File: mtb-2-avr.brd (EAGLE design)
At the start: 27 x 22 mm, 17 parts, among them IC1 MEGA8A-AU, Q1 14.745 MHz

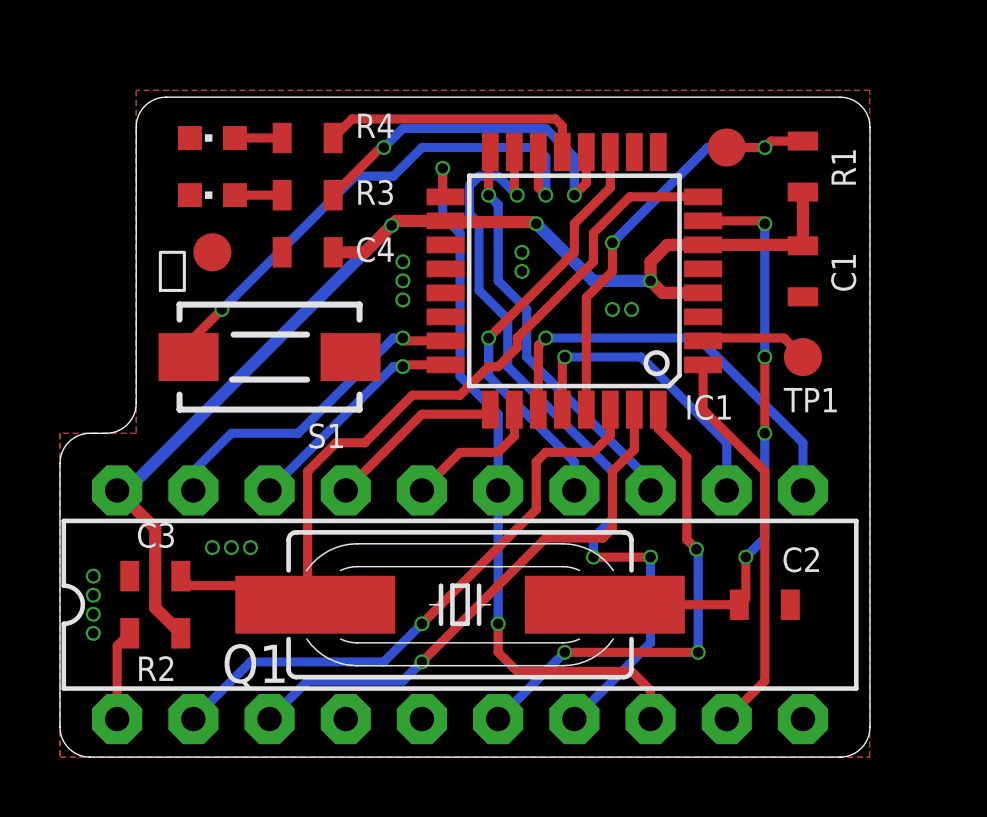
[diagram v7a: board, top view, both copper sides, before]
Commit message: Add possibility for THT crystal.
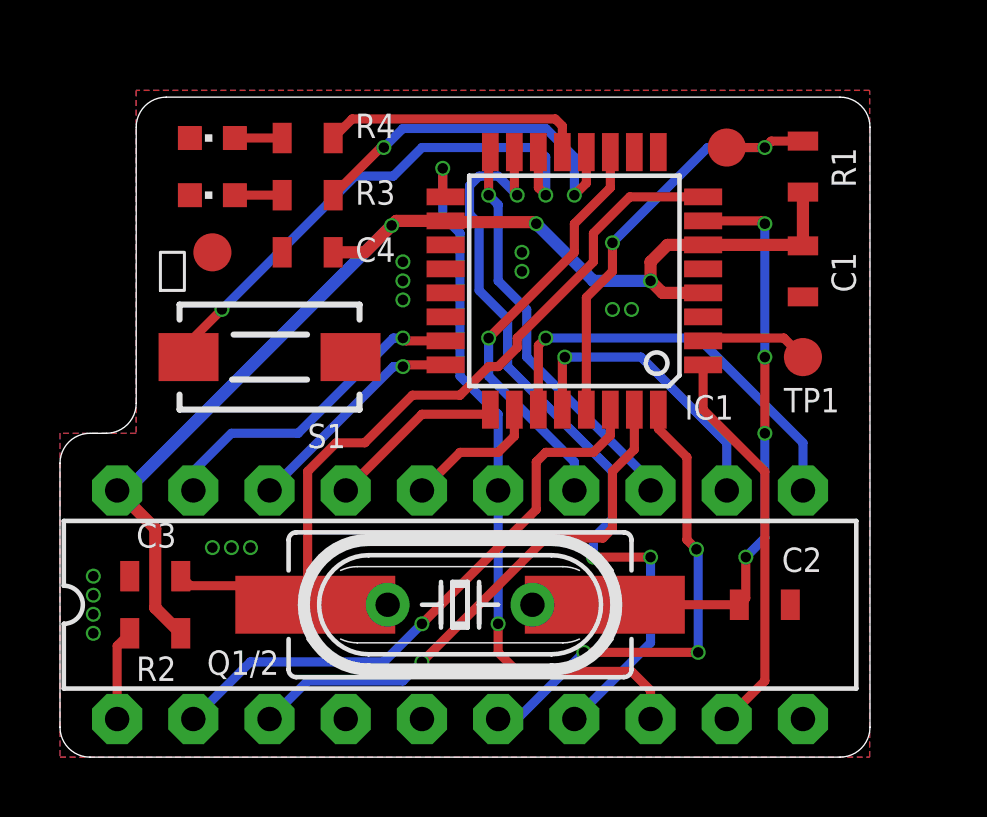
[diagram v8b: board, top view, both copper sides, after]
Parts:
- added Q2: 14.745 MHz, crystal:HC49/S
- renumbered Q1 to Q1/2
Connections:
- removed net N$1: C2.2, IC1.7, Q1/2.2
- removed net N$2: C3.2, IC1.8, Q1/2.1
- new net CRYST+: C2.2, IC1.7, Q1/2.2, Q2.2
- new net CRYST-: C3.2, IC1.8, Q1/2.1, Q2.1
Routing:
- net CRYST-: track 0.00 -> 29.6 mm
- net N$2: track 27.1 -> 0.00 mm
- net CRYST+: track 0.00 -> 22.0 mm, vias 0 -> 4
- net N$1: track 19.6 -> 0.00 mm, vias 4 -> 0
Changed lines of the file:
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@@
 <layer number="14" name="Route14" color="22" fill="1" visible="no" active="no"/>
 <layer number="15" name="Route15" color="23" fill="1" visible="no" active="no"/>
-<layer number="16" name="Bottom" color="4" fill="1" visible="no" active="yes"/>
+<layer number="16" name="Bottom" color="4" fill="1" visible="yes" active="yes"/>
 <layer number="17" name="Pads" color="2" fill="1" visible="yes" active="yes"/>
 <layer number="18" name="Vias" color="2" fill="1" visible="yes" active="yes"/>
-<layer number="19" name="Unrouted" color="6" fill="1" visible="no" active="yes"/>
+<layer number="19" name="Unrouted" color="6" fill="1" visible="yes" active="yes"/>
 <layer number="20" name="Dimension" color="24" fill="1" visible="yes" active="yes"/>
 <layer number="21" name="tPlace" color="7" fill="1" visible="yes" active="yes"/>
-<layer number="22" name="bPlace" color="7" fill="1" visible="no" active="yes"/>
-<layer number="23" name="tOrigins" color="15" fill="1" visible="no" active="yes"/>
-<layer number="24" name="bOrigins" color="15" fill="1" visible="no" active="yes"/>
-<layer number="25" name="tNames" color="7" fill="1" visible="yes" active="yes"/>
+<layer number="22" name="bPlace" color="7" fill="1" visible="yes" active="yes"/>
+<layer number="23" name="tOrigins" color="15" fill="1" visible="yes" active="yes"/>
+<layer number="24" name="bOrigins" color="15" fill="1" visible="yes" active="yes"/>
+<layer number="25" name="tNames" color="7" fill="1" visible="no" active="yes"/>
 <layer number="26" name="bNames" color="7" fill="1" visible="no" active="yes"/>
 <layer number="27" name="tValues" color="7" fill="1" visible="no" active="yes"/>
@@
 <layer number="44" name="Drills" color="7" fill="1" visible="no" active="yes"/>
 <layer number="45" name="Holes" color="7" fill="1" visible="no" active="yes"/>
-<layer number="46" name="Milling" color="3" fill="1" visible="no" active="yes"/>
+<layer number="46" name="Milling" color="3" fill="1" visible="yes" active="yes"/>
 <layer number="47" name="Measures" color="7" fill="1" visible="no" active="yes"/>
 <layer number="48" name="Document" color="7" fill="1" visible="no" active="yes"/>
-<layer number="49" name="Reference" color="7" fill="1" visible="no" active="yes"/>
+<layer number="49" name="Reference" color="7" fill="1" visible="yes" active="yes"/>
 <layer number="50" name="dxf" color="7" fill="1" visible="no" active="no"/>
 <layer number="51" name="tDocu" color="7" fill="1" visible="yes" active="yes"/>
-<layer number="52" name="bDocu" color="7" fill="1" visible="no" active="yes"/>
+<layer number="52" name="bDocu" color="7" fill="1" visible="yes" active="yes"/>
 <layer number="53" name="tGND_GNDA" color="7" fill="9" visible="no" active="no"/>
 <layer number="54" name="bGND_GNDA" color="1" fill="9" visible="no" active="no"/>
@@
 <wire x1="27" y1="21" x2="26" y2="22" width="0" layer="20" curve="90"/>
 <wire x1="26" y1="0" x2="27" y2="1" width="0" layer="20" curve="90"/>
-<text x="6.985" y="3.81" size="1.016" layer="22" rot="MR0" align="bottom-center">MTB-UNI
+<text x="6.985" y="18.0975" size="1.016" layer="22" rot="MR0" align="bottom-center">MTB-UNI
 v2 upgrade</text>
 <text x="24.765" y="16.51" size="1.016" layer="22" rot="MR90" align="bottom-center">v1.0 JH 2021</text>
@@
 </attributes>
 <variantdefs>
+<variantdef name="CRYSTAL_THT"/>
+<variantdef name="CRYSTAL_SMD"/>
 </variantdefs>
 <classes>
@@
 <attribute name="POPULARITY" value="28" x="5.08" y="20.6375" size="1.778" layer="27" rot="R90" display="off"/>
 </element>
-<element name="Q1" library="crystal" library_urn="urn:adsk.eagle:library:204" package="HC49UP" package3d_urn="urn:adsk.eagle:package:12078/1" value="14.745 MHz" x="13.335" y="5.08" smashed="yes">
+<element name="Q1/2" library="crystal" library_urn="urn:adsk.eagle:library:204" package="HC49UP" package3d_urn="urn:adsk.eagle:package:12078/1" value="14.745 MHz" x="13.335" y="5.08" smashed="yes">
 <attribute name="LCSC_PART" value="C19646" x="13.335" y="5.08" size="1.778" layer="27" display="off"/>
 <attribute name="MF" value="" x="13.335" y="5.08" size="1.778" layer="27" display="off"/>
 <attribute name="MPN" value="" x="13.335" y="5.08" size="1.778" layer="27" display="off"/>
-<attribute name="NAME" x="5.3975" y="2.4765" size="1.27" layer="25" ratio="10"/>
+<attribute name="NAME" x="7.3025" y="3.556" size="0.8128" layer="25" ratio="10" rot="R180"/>
 <attribute name="OC_FARNELL" value="unknown" x="13.335" y="5.08" size="1.778" layer="27" display="off"/>
 <attribute name="OC_NEWARK" value="unknown" x="13.335" y="5.08" size="1.778" layer="27" display="off"/>
@@
 <attribute name="TP_SIGNAL_NAME" value="" x="5.08" y="16.8275" size="1.778" layer="27" display="off"/>
 <attribute name="VALUE" x="4.445" y="16.0655" size="0.0254" layer="27"/>
+</element>
+<element name="Q2" library="crystal" library_urn="urn:adsk.eagle:library:204" package="HC49/S" package3d_urn="urn:adsk.eagle:package:12071/1" value="14.745 MHz" x="13.335" y="5.08" smashed="yes">
+<attribute name="MF" value="" x="13.335" y="5.08" size="1.778" layer="27" display="off"/>
+<attribute name="MPN" value="" x="13.335" y="5.08" size="1.778" layer="27" display="off"/>
+<attribute name="OC_FARNELL" value="1667008" x="13.335" y="5.08" size="1.778" layer="27" display="off"/>
+<attribute name="OC_NEWARK" value="unknown" x="13.335" y="5.08" size="1.778" layer="27" display="off"/>
+<attribute name="POPULARITY" value="49" x="13.335" y="5.08" size="1.778" layer="27" display="off"/>
+<attribute name="VALUE" x="8.255" y="1.143" size="1.27" layer="27" ratio="10"/>
 </element>
 </elements>
@@
 <via x="21.215" y="6.9275" extent="1-16" drill="0.35"/>
 <via x="21.2725" y="3.4925" extent="1-16" drill="0.35"/>
-<wire x1="21.2725" y1="3.4925" x2="16.8275" y2="3.4925" width="0.3048" layer="1"/>
+<wire x1="21.2725" y1="3.4925" x2="17.4625" y2="3.4925" width="0.3048" layer="1"/>
 <wire x1="21.215" y1="6.9275" x2="21.2725" y2="6.87" width="0.3048" layer="16"/>
 <wire x1="21.2725" y1="6.87" x2="21.2725" y2="3.4925" width="0.3048" layer="16"/>
-<wire x1="14.605" y1="1.27" x2="16.8275" y2="3.4925" width="0.3048" layer="16"/>
-<via x="16.8275" y="3.4925" extent="1-16" drill="0.35"/>
+<wire x1="14.605" y1="1.27" x2="15.24" y2="1.27" width="0.3048" layer="16"/>
+<wire x1="17.4625" y1="3.4925" x2="15.24" y2="1.27" width="0.3048" layer="16"/>
+<via x="17.4625" y="3.4925" extent="1-16" drill="0.35"/>
 </signal>
 <signal name="OUT_SET">
@@
 <via x="16.8275" y="13.335" extent="1-16" drill="0.35"/>
 </signal>
-<signal name="N$1">
+<signal name="CRYST+">
 <contactref element="C2" pad="2"/>
-<contactref element="Q1" pad="2"/>
+<contactref element="Q1/2" pad="2"/>
 <contactref element="IC1" pad="7"/>
 <wire x1="18.161" y1="5.08" x2="22.645" y2="5.08" width="0.3048" layer="1"/>
@@
 <wire x1="22.645" y1="5.08" x2="22.86" y2="5.295" width="0.3048" layer="1"/>
 <wire x1="22.86" y1="6.6675" x2="22.86" y2="5.295" width="0.3048" layer="1"/>
-</signal>
-<signal name="N$2">
+<contactref element="Q2" pad="2"/>
+<wire x1="18.161" y1="5.08" x2="15.748" y2="5.08" width="0.3048" layer="1"/>
+</signal>
+<signal name="CRYST-">
 <contactref element="IC1" pad="8"/>
-<contactref element="Q1" pad="1"/>
+<contactref element="Q1/2" pad="1"/>
 <contactref element="C3" pad="2"/>
 <wire x1="8.509" y1="5.08" x2="7.874" y2="5.715" width="0.3048" layer="1"/>
@@
 <wire x1="9.2075" y1="10.4775" x2="10.16" y2="10.4775" width="0.3048" layer="1"/>
 <wire x1="10.16" y1="10.4775" x2="11.7475" y2="12.065" width="0.3048" layer="1"/>
+<contactref element="Q2" pad="1"/>
+<wire x1="8.509" y1="5.08" x2="10.922" y2="5.08" width="0.3048" layer="1"/>
 </signal>
 <signal name="RESET">
@@
 <mfgpreviewcolor name="substratecolor" color="0xFF786E46"/>
 </mfgpreviewcolors>
+<errors>
+</errors>
 </board>
 </drawing>
